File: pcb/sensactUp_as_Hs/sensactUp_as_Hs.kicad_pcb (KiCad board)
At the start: 2 copper layers, 100 x 86.5 mm, 42 parts, among them J1 EXT_ROT, J2 SensactBusConnector, J3 24V+CAN IN, J4 24V+CAN OUT, J5 24V+CAN OUT, J6 24V+CAN OUT, J7 12V LED, Q1 AO3400A, Q2 AO3400A, Q3 AO3400A, SW1 EC11, SW3 TERM OFF, U1 DS18B20, U2 ESP32-S3-DevKitC, U3 DCDC_MP2315, U4 DCDC_MP2315, U5 SN65HVD230, U6 PCA9685PW

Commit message: sensactUp-as_HS updates
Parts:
- added C6: u1, Capacitor_SMD:C_0805_2012Metric_Pad1.18x1.45mm_HandSolder, B.Cu at (120.3, 91.0)
- added C7: 1u, Capacitor_SMD:C_0805_2012Metric_Pad1.18x1.45mm_HandSolder, B.Cu at (118.2, 91.0)
- added J10: OUT0-3, liebler_CONN:PhoenixContact_MCV_1,5_4-G-3.5_1x04_P3.50mm_Vertical_smallerCourtyard, F.Cu at (111.7, 113.1)
- added J11: OUT0-3, liebler_CONN:PhoenixContact_MCV_1,5_4-G-3.5_1x04_P3.50mm_Vertical_smallerCourtyard, F.Cu at (140.9, 113.1)
- added J12: OUT0-3, liebler_CONN:PhoenixContact_MC_1,5_4-G-3.5_1x04_P3.50mm_Horizontal_smallerCourtyard, F.Cu at (141.0, 64.8)
- added J13: OUT0-3, liebler_CONN:PhoenixContact_MCV_1,5_4-G-3.5_1x04_P3.50mm_Vertical_smallerCourtyard, F.Cu at (141.0, 83.3)
- added J14: OUT0-3, liebler_CONN:PhoenixContact_MCV_1,5_4-G-3.5_1x04_P3.50mm_Vertical_smallerCourtyard, F.Cu at (111.7, 83.9)
- added J15: Conn_01x04, Connector_PinHeader_2.54mm:PinHeader_1x04_P2.54mm_Vertical, F.Cu at (137.1, 118.0)
- added J16: Conn_01x04, Connector_PinHeader_2.54mm:PinHeader_1x04_P2.54mm_Vertical, F.Cu at (107.9, 118.0)
- added J17: Conn_01x04, Connector_PinHeader_2.54mm:PinHeader_1x04_P2.54mm_Vertical, F.Cu at (107.9, 103.4)
- added J18: Conn_01x04, Connector_PinHeader_2.54mm:PinHeader_1x04_P2.54mm_Vertical, F.Cu at (115.5, 61.6)
- added J19: Conn_01x04, Connector_PinHeader_2.54mm:PinHeader_1x04_P2.54mm_Vertical, F.Cu at (144.8, 67.8)
- added J20: Conn_01x04, Connector_PinHeader_2.54mm:PinHeader_1x04_P2.54mm_Vertical, F.Cu at (137.2, 88.2)
- added J21: Conn_01x04, Connector_PinHeader_2.54mm:PinHeader_1x04_P2.54mm_Vertical, F.Cu at (107.9, 88.8)
- added J8: OUT0-3, liebler_CONN:PhoenixContact_MCV_1,5_4-G-3.5_1x04_P3.50mm_Vertical_smallerCourtyard, F.Cu at (140.9, 97.9)
- added J9: OUT0-3, liebler_CONN:PhoenixContact_MCV_1,5_4-G-3.5_1x04_P3.50mm_Vertical_smallerCourtyard, F.Cu at (111.7, 98.5)
- added U7: PCA9555PW, liebler_SEMICONDUCTORS:TSSOP-24_4.4x7.8mm_Pitch0.65mm_handsolder, B.Cu at (114.6, 74.0)
- J1: value EXT_ROT -> Conn_01x04; footprint Connector_Phoenix_MC:PhoenixContact_MCV_1,5_4-G-3.5_1x04_P3.50mm_Vertical -> Connector_PinHeader_2.54mm:PinHeader_1x04_P2.54mm_Vertical
- J5: value 24V+CAN OUT -> EXT_ENC
- J6: value 24V+CAN OUT -> OUT0-3
- R8, R9: value 10k -> 4k7
- U6: footprint Package_SO:TSSOP-28_4.4x9.7mm_P0.65mm -> liebler_SEMICONDUCTORS:TSSOP-28_4.4x9.7mm_Pitch0.65mm_handsolder
- moved J7 70.5 mm to (140.9, 135.3), turned to 0 degrees
- moved U4 69.7 mm to (126.0, 119.4)
- moved Q1 63.4 mm to (138.6, 131.0), turned to -90 degrees
- moved Q3 63.2 mm to (146.6, 131.0), turned to -90 degrees
- moved Q2 62.3 mm to (142.6, 131.0), turned to -90 degrees
- moved R12 60.3 mm to (138.6, 127.3), turned to 0 degrees
- moved R16 54.9 mm to (146.6, 127.3), turned to 0 degrees
- moved R14 54.0 mm to (142.6, 127.3), turned to 0 degrees
- moved R15 50.6 mm to (145.6, 124.4), turned to -90 degrees
- moved J1 47.9 mm to (137.1, 102.8), turned to 90 degrees
- moved R13 47.4 mm to (141.7, 124.4), turned to -90 degrees
- moved R11 47.2 mm to (137.6, 124.4), turned to -90 degrees
- moved R7 45.2 mm to (103.1, 78.0), turned to 90 degrees
- moved U1 40.3 mm to (100.2, 79.6), turned to 90 degrees
- moved C5 16.0 mm to (108.2, 76.7), turned to 180 degrees
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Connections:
- J1 pad 1: /A -> /L2
- J1 pad 2: GND -> /L1
- J1 pad 3: /B -> /L0
- J1 pad 4: /S -> GND
- J5 pad 1: unconnected-(J5-Pin_1-Pad1) -> ROT_A
- J5 pad 2: unconnected-(J5-Pin_2-Pad2) -> ROT_B
- J5 pad 3: unconnected-(J5-Pin_3-Pad3) -> PROG_IO0
- J5 pad 4: unconnected-(J5-Pin_4-Pad4) -> GND
- J6 pad 1: unconnected-(J6-Pin_1-Pad1) -> /T2
- J6 pad 2: unconnected-(J6-Pin_2-Pad2) -> /T1
- J6 pad 3: unconnected-(J6-Pin_3-Pad3) -> /T0
- J6 pad 4: unconnected-(J6-Pin_4-Pad4) -> GND
- R11 pad 1: PWM0 -> /L8
- R13 pad 1: PWM1 -> /L7
- R15 pad 1: PWM2 -> /L6
- U2 pad 35: unconnected-(U2-GPIO38-Pad35) -> Onewire
- U2 pad 40: unconnected-(U2-GPIO2/ADC1_CH1-Pad40) -> SDA
- U2 pad 41: unconnected-(U2-GPIO1/ADC1_CH0-Pad41) -> SCL
- U6 pad 10: unconnected-(U6-LED4-Pad10) -> /L4
- U6 pad 11: unconnected-(U6-LED5-Pad11) -> /L5
- U6 pad 12: unconnected-(U6-LED6-Pad12) -> /L6
- U6 pad 13: unconnected-(U6-LED7-Pad13) -> /L7
- U6 pad 15: unconnected-(U6-LED8-Pad15) -> /L8
- U6 pad 16: unconnected-(U6-LED9-Pad16) -> /L9
- U6 pad 17: unconnected-(U6-LED10-Pad17) -> /L10
- U6 pad 18: unconnected-(U6-LED11-Pad18) -> /L11
- U6 pad 19: unconnected-(U6-LED12-Pad19) -> /L12
- U6 pad 20: unconnected-(U6-LED13-Pad20) -> /L13
- U6 pad 21: unconnected-(U6-LED14-Pad21) -> /L14
- U6 pad 22: unconnected-(U6-LED15-Pad22) -> /L15
- U6 pad 6: unconnected-(U6-LED0-Pad6) -> /L0
- U6 pad 7: unconnected-(U6-LED1-Pad7) -> /L1
- U6 pad 8: unconnected-(U6-LED2-Pad8) -> /L2
- U6 pad 9: unconnected-(U6-LED3-Pad9) -> /L3
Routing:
- net +3V3: track 25.7 -> 233.6 mm, vias 0 -> 4
- net SDA: track 0.00 -> 145.2 mm
- net SCL: track 0.00 -> 143.4 mm
- net +24V: track 75.2 -> 174.8 mm
- net PROG_IO0: track 1.90 -> 93.2 mm
- net ROT_B: track 2.43 -> 51.6 mm
- net /T6: track 0.00 -> 42.3 mm
- net /T7: track 0.00 -> 39.3 mm
- net GND: track 2.53 -> 39.6 mm, vias 0 -> 111
- net /T5: track 0.00 -> 36.9 mm
- net /L6: track 0.00 -> 35.3 mm
- net Onewire: track 0.00 -> 35.3 mm
- net /T4: track 0.00 -> 34.4 mm
- net ROT_A: track 2.41 -> 35.9 mm
- net /L8: track 0.00 -> 33.3 mm
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- added copper zone on B.Cu, net GND
- added copper zone on F.Cu, net GND
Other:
- board text added: "12V"
- board text added: "24V"
- board text added: "CANH"
- board text added: "CANL"
- board text added: "GND"
- board text added: "L0"
- board text added: "L1"
- board text added: "L10"
- board text added: "L11"
- board text added: "L12"
- board text added: "L13"
- board text added: "L14"
- board text added: "L2"
- board text added: "L3"
- board text added: "L4"
- board text added: "L5"
- board text added: "L6"
- board text added: "L7"
- board text added: "L8"
- board text added: "L9"
- board text added: "ON TERM OFF"
- board text added: "ROTA"
- board text added: "ROTB"
- board text added: "SW"
- board text added: "T0"
- board text added: "T1"
- board text added: "T10"
- board text added: "T11"
- board text added: "T2"
- board text added: "T3"
- board text added: "T4"
- board text added: "T5"
- board text added: "T6"
- board text added: "T7"
- board text added: "T8"
- board text added: "T9"

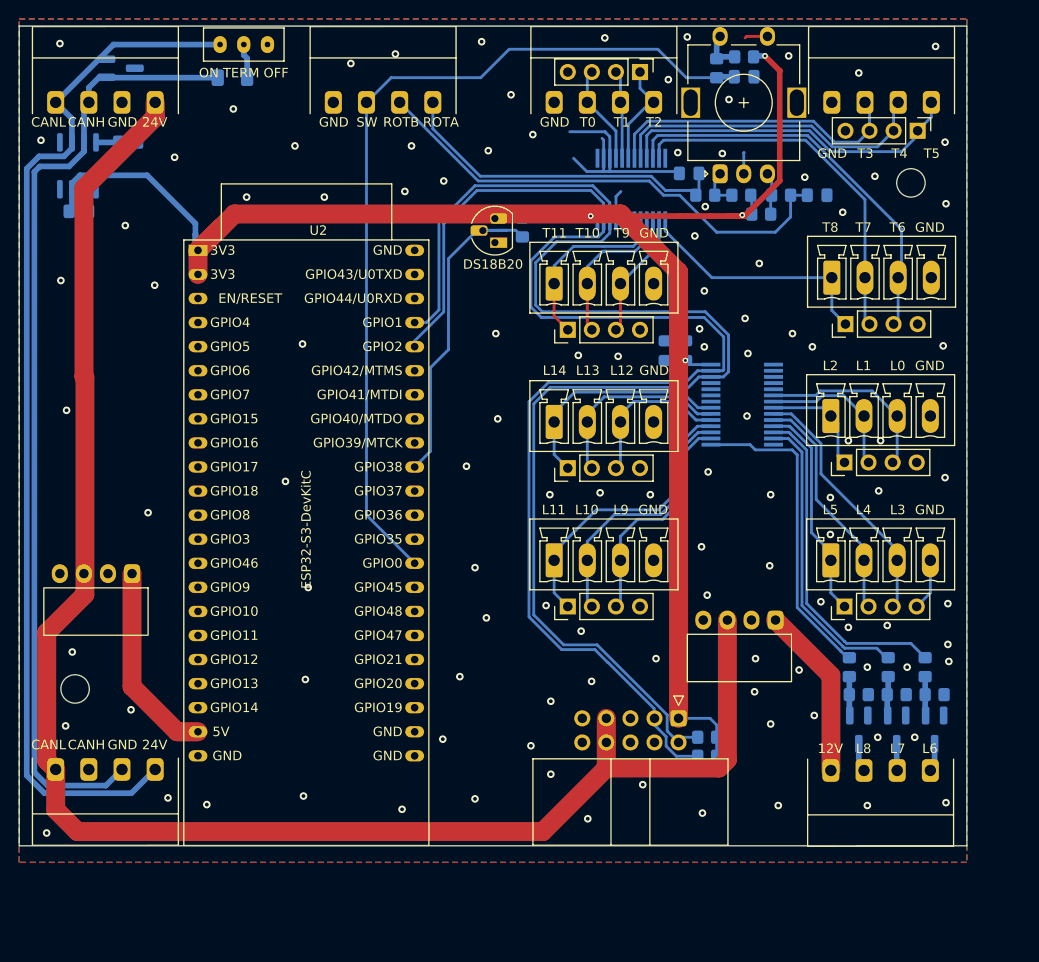
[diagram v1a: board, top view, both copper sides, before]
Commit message: Pin usage according to sensactRingEncoder
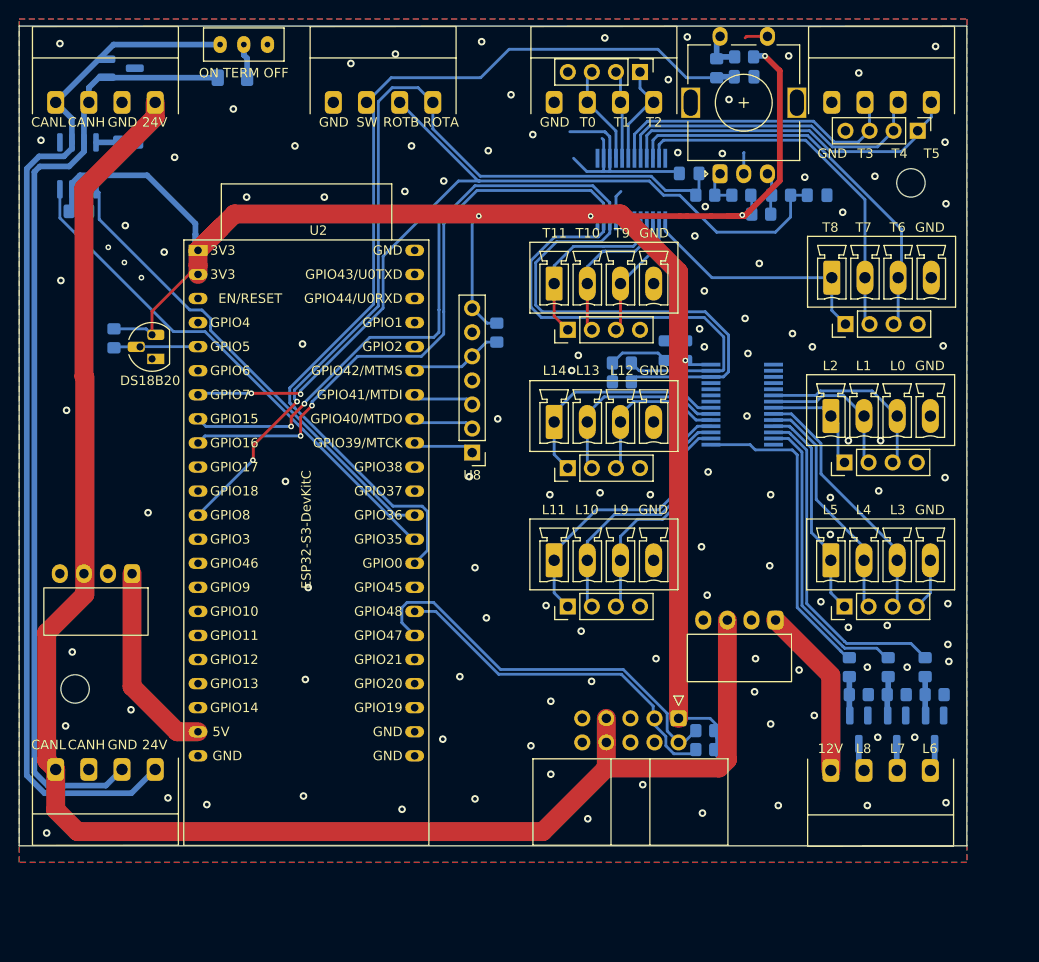
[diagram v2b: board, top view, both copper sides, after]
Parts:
- added R18: 1M, Resistor_SMD:R_0805_2012Metric_Pad1.20x1.40mm_HandSolder, B.Cu at (100.4, 89.1)
- added R19: 4k7, Resistor_SMD:R_0805_2012Metric_Pad1.20x1.40mm_HandSolder, B.Cu at (122.4, 133.1)
- added R20: 4k7, Resistor_SMD:R_0805_2012Metric_Pad1.20x1.40mm_HandSolder, B.Cu at (122.4, 131.1)
- added U8: MAX98357_MODULE, Connector_PinHeader_2.54mm:PinHeader_1x07_P2.54mm_Vertical, F.Cu at (97.8, 101.8)
- moved R7 44.7 mm to (60.0, 89.7)
- moved R9 42.5 mm to (113.6, 92.3), turned to 0 degrees
- moved R8 38.6 mm to (113.6, 94.3), turned to 0 degrees
- moved U1 38.2 mm to (64.0, 91.9)
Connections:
- J2 pad 2: SCL -> SCL_EXT
- J2 pad 3: SDA -> SDA_EXT
- U2 pad 10: unconnected-(U2-GPIO17/ADC2_CH6-Pad10) -> LCD_TRST
- U2 pad 11: unconnected-(U2-GPIO18/ADC2_CH7-Pad11) -> LCD_TINT
- U2 pad 12: unconnected-(U2-GPIO8/ADC1_CH7-Pad12) -> ROT_A
- U2 pad 15: unconnected-(U2-GPIO9/ADC1_CH8-Pad15) -> LCD_BL
- U2 pad 16: unconnected-(U2-GPIO10/ADC1_CH9-Pad16) -> LCD_RS
- U2 pad 17: unconnected-(U2-GPIO11/ADC2_CH0-Pad17) -> LCD_CS
- U2 pad 18: unconnected-(U2-GPIO12/ADC2_CH1-Pad18) -> LCD_SCK
- U2 pad 19: unconnected-(U2-GPIO13/ADC2_CH2-Pad19) -> LCD_DAT
- U2 pad 20: unconnected-(U2-GPIO14/ADC2_CH3-Pad20) -> LCD_RESET
- U2 pad 27: unconnected-(U2-GPIO21-Pad27) -> BaseIO1
- U2 pad 28: unconnected-(U2-GPIO47-Pad28) -> SCL_EXT
- U2 pad 29: unconnected-(U2-GPIO48-Pad29) -> SDA_EXT
- U2 pad 32: unconnected-(U2-GPIO35-Pad32) -> CAN_RX
- U2 pad 33: unconnected-(U2-GPIO36-Pad33) -> CAN_TX
- U2 pad 35: Onewire -> unconnected-(U2-GPIO38-Pad35)
- U2 pad 36: unconnected-(U2-GPIO39/MTCK-Pad36) -> I2S_FS
- U2 pad 37: unconnected-(U2-GPIO40/MTDO-Pad37) -> I2S_BCLK
- U2 pad 38: unconnected-(U2-GPIO41/MTDI-Pad38) -> I2S_DAC
- U2 pad 39: unconnected-(U2-GPIO42/MTMS-Pad39) -> AMP_SD
- U2 pad 40: SDA -> MIC_CLK
- U2 pad 41: SCL -> MIC_DAT
- U2 pad 5: unconnected-(U2-GPIO5/ADC1_CH4-Pad5) -> Onewire
- U2 pad 7: unconnected-(U2-GPIO7/ADC1_CH6-Pad7) -> ROT_B
- U2 pad 8: unconnected-(U2-GPIO15/ADC2_CH4/32K_P-Pad8) -> SCL
- U2 pad 9: unconnected-(U2-GPIO16/ADC2_CH5/32K_N-Pad9) -> SDA
- U5 pad 1: CANT -> CAN_TX
- U5 pad 4: CANR -> CAN_RX
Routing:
- net ROT_A: track 35.9 -> 94.6 mm, vias 0 -> 2
- net CAN_RX: track 0.00 -> 54.5 mm
- net CAN_TX: track 0.00 -> 52.2 mm
- net ROT_B: track 51.6 -> 94.2 mm, vias 0 -> 2
- net SCL_EXT: track 0.00 -> 42.0 mm
- net SDA_EXT: track 0.00 -> 37.4 mm
- net +3V3: track 233.6 -> 266.0 mm, vias 4 -> 5
- net SDA: track 145.2 -> 114.7 mm, vias 0 -> 2
- net SCL: track 143.4 -> 115.6 mm, vias 0 -> 2
- net Onewire: track 35.3 -> 8.92 mm
- net PROG_IO0: track 93.2 -> 103.4 mm
- net AMP_SD: track 0.00 -> 9.92 mm
- net I2S_FS: track 0.00 -> 6.49 mm
- net I2S_DAC: track 0.00 -> 6.49 mm
- net I2S_BCLK: track 0.00 -> 6.49 mm
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
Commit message: sensactUp_as_Hs
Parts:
- removed C7: 1u, Capacitor_SMD:C_0805_2012Metric_Pad1.18x1.45mm_HandSolder
- removed J1, J15, J16, J17, J18, J19, J20, J21: Conn_01x04, Connector_PinHeader_2.54mm:PinHeader_1x04_P2.54mm_Vertical
- removed J13, J14: OUT0-3, liebler_CONN:PhoenixContact_MCV_1,5_4-G-3.5_1x04_P3.50mm_Vertical_smallerCourtyard
- removed Q1, Q2, Q3: AO3400A, Package_TO_SOT_SMD:SOT-23_Handsoldering
- removed SW1: EC11, liebler_MECH:RotaryEncoder_Alps_EC11E-Switch_Vertical_H20mm
- removed U6: PCA9685PW, liebler_SEMICONDUCTORS:TSSOP-28_4.4x9.7mm_Pitch0.65mm_handsolder
- added C10: 10n, Capacitor_SMD:C_0805_2012Metric_Pad1.18x1.45mm_HandSolder, B.Cu at (72.0, 103.8)
- added C11: 10n, Capacitor_SMD:C_0805_2012Metric_Pad1.18x1.45mm_HandSolder, B.Cu at (72.0, 93.7)
- added C12: 10n, Capacitor_SMD:C_0805_2012Metric_Pad1.18x1.45mm_HandSolder, B.Cu at (72.0, 101.3)
- added C8: u1, Capacitor_SMD:C_0805_2012Metric_Pad1.18x1.45mm_HandSolder, B.Cu at (102.4, 67.3)
- added C9: u1, Capacitor_SMD:C_0805_2012Metric_Pad1.18x1.45mm_HandSolder, B.Cu at (119.5, 66.2)
- added U10: TPL7407LAPW, Package_SO:TSSOP-16_4.4x5mm_P0.65mm, B.Cu at (123.2, 72.3)
- added U11: DS2482, liebler_SEMICONDUCTORS:SOIC-8_3.9x4.9mm_P1.27mm_handsolder, B.Cu at (98.8, 111.5)
- added U9: TPL7407LAPW, Package_SO:TSSOP-16_4.4x5mm_P0.65mm, B.Cu at (106.8, 72.3)
- J10: value OUT0-3 -> ROT1; footprint liebler_CONN:PhoenixContact_MCV_1,5_4-G-3.5_1x04_P3.50mm_Vertical_smallerCourtyard -> liebler_CONN:PhoenixContact_MCV_1,5_5-G-3.81_1x05_P3.81mm_Vertical_smallerCourtyard
- J11: value OUT0-3 -> OneWire; footprint liebler_CONN:PhoenixContact_MCV_1,5_4-G-3.5_1x04_P3.50mm_Vertical_smallerCourtyard -> liebler_CONN:PhoenixContact_MCV_1,5_5-G-3.81_1x05_P3.81mm_Vertical_smallerCourtyard
- J12: value OUT0-3 -> LED Driver; footprint liebler_CONN:PhoenixContact_MC_1,5_4-G-3.5_1x04_P3.50mm_Horizontal_smallerCourtyard -> Connector_PinHeader_2.54mm:PinHeader_1x08_P2.54mm_Vertical
- J3: footprint liebler_CONN:PhoenixContact_MC_1,5_4-G-3.5_1x04_P3.50mm_Horizontal_smallerCourtyard -> liebler_CONN:PhoenixContact_MCV_1,5_4-G-3.5_1x04_P3.50mm_Vertical_smallerCourtyard
- J4: value 24V+CAN OUT -> LED; footprint liebler_CONN:PhoenixContact_MC_1,5_4-G-3.5_1x04_P3.50mm_Horizontal_smallerCourtyard -> liebler_CONN:PhoenixContact_MCV_1,5_5-G-3.81_1x05_P3.81mm_Vertical_smallerCourtyard
- J5: value EXT_ENC -> ROT2; footprint liebler_CONN:PhoenixContact_MC_1,5_4-G-3.5_1x04_P3.50mm_Horizontal_smallerCourtyard -> liebler_CONN:PhoenixContact_MCV_1,5_5-G-3.81_1x05_P3.81mm_Vertical_smallerCourtyard
- J6: value OUT0-3 -> LED Driver; footprint liebler_CONN:PhoenixContact_MC_1,5_4-G-3.5_1x04_P3.50mm_Horizontal_smallerCourtyard -> liebler_CONN:PhoenixContact_MC_0,5_8-G-2.5_1x08_P2.50mm_Horizontal
- J7: value 12V LED -> LED; footprint liebler_CONN:PhoenixContact_MC_1,5_4-G-3.5_1x04_P3.50mm_Horizontal_smallerCourtyard -> liebler_CONN:PhoenixContact_MCV_1,5_5-G-3.81_1x05_P3.81mm_Vertical_smallerCourtyard
- J8, J9: value OUT0-3 -> LED; footprint liebler_CONN:PhoenixContact_MCV_1,5_4-G-3.5_1x04_P3.50mm_Vertical_smallerCourtyard -> liebler_CONN:PhoenixContact_MCV_1,5_5-G-3.81_1x05_P3.81mm_Vertical_smallerCourtyard
- R11, R13, R15: value k1 -> 10k
- U2: footprint Espressif:ESP32-S3-DevKitC -> liebler_MODULES:ESP32-S3 chinese dev board
- U3, U4: footprint liebler_MODULES:DCDC_MP2315 -> liebler_MODULES:DCDC_MP2315_horizontal
- U7: value PCA9555PW -> PCA9685PW; footprint liebler_SEMICONDUCTORS:TSSOP-24_4.4x7.8mm_Pitch0.65mm_handsolder -> liebler_SEMICONDUCTORS:TSSOP-28_4.4x9.7mm_Pitch0.65mm_handsolder
- moved J4 114.6 mm to (145.6, 60.1), turned to 180 degrees
- moved R14 92.7 mm to (63.1, 79.6), turned to 180 degrees
- moved R16 92.1 mm to (62.8, 89.2), turned to 180 degrees
- moved R13 91.4 mm to (63.1, 77.7), turned to 180 degrees
- moved R15 89.2 mm to (62.8, 91.1), turned to 180 degrees
- moved R12 83.2 mm to (62.8, 93.0), turned to 180 degrees
- moved R11 80.4 mm to (62.8, 94.9), turned to 180 degrees
- moved J7 77.4 mm to (122.6, 60.1), turned to 180 degrees
- moved SW3 75.7 mm to (62.3, 133.6), turned to 0 degrees
- moved D1 75.7 mm to (55.9, 136.7), turned to 180 degrees
- moved R17 75.4 mm to (61.1, 136.7)
- moved J3 75.0 mm to (59.4, 139.8), turned to 0 degrees
- moved J6 71.5 mm to (127.7, 134.5), turned to 0 degrees
- moved R4 68.5 mm to (62.8, 96.8), turned to 180 degrees
- moved R2 68.1 mm to (63.1, 85.3)
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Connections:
- C1 pad 2: ROT_A -> ROT2_A
- C2 pad 2: ROT_B -> ROT1_A
- C3 pad 1: PROG_IO0 -> GND
- C3 pad 2: GND -> ROT1_B
- J10 pad 1: /L11 -> GND
- J10 pad 2: /L10 -> GND
- J10 pad 3: /L9 -> ROT1_SS
- J10 pad 4: GND -> ROT1_BB
- J11 pad 1: /L5 -> +24V
- J11 pad 2: /L4 -> +12V
- J11 pad 3: /L3 -> +3V3
- J11 pad 4: GND -> Net-(J11-Pin_4)
- J12 pad 1: /T5 -> /L5
- J12 pad 2: /T4 -> /L4
- J12 pad 3: /T3 -> /L3
- J12 pad 4: GND -> /L2
- J3 pad 1: +24V -> GND
- J3 pad 2: GND -> CANL
- J3 pad 4: CANL -> +24V
- J4 pad 1: +24V -> LED11
- J4 pad 2: GND -> LED10
- J4 pad 3: CANH -> LED9
- J4 pad 4: CANL -> LED8
- J5 pad 1: ROT_A -> GND
- J5 pad 2: ROT_B -> GND
- J5 pad 3: PROG_IO0 -> ROT2_SS
- J5 pad 4: GND -> ROT2_BB
- J6 pad 1: /T2 -> /L5
- J6 pad 2: /T1 -> /L4
- J6 pad 3: /T0 -> /L3
- J6 pad 4: GND -> /L2
- J7 pad 1: +12V -> LED7
- J7 pad 2: Net-(J7-Pin_2) -> LED6
- J7 pad 3: Net-(J7-Pin_3) -> LED5
- J7 pad 4: Net-(J7-Pin_4) -> LED4
- J8 pad 1: /L2 -> LED12
- J8 pad 2: /L1 -> LED13
- J8 pad 3: /L0 -> LED_G_14
- J8 pad 4: GND -> LED_G_15
- J9 pad 1: /L14 -> LED3
- J9 pad 2: /L13 -> LED2
- J9 pad 3: /L12 -> LED1
- J9 pad 4: GND -> LED0
- R1 pad 1: ROT_A -> ROT2_A
- R1 pad 2: /A -> ROT2_AA
- R11 pad 1: /L8 -> ROT2_B
- R11 pad 2: Net-(Q1-G) -> ROT2_BB
- R12 pad 1: Net-(Q1-G) -> +3V3
- R12 pad 2: GND -> ROT2_BB
- R13 pad 1: /L7 -> ROT1_S
- R13 pad 2: Net-(Q2-G) -> ROT1_SS
- R14 pad 1: Net-(Q2-G) -> +3V3
- R14 pad 2: GND -> ROT1_SS
- R15 pad 1: /L6 -> ROT2_S
- R15 pad 2: Net-(Q3-G) -> ROT2_SS
- R16 pad 1: Net-(Q3-G) -> +3V3
- R16 pad 2: GND -> ROT2_SS
- R2 pad 1: ROT_B -> ROT1_A
- R2 pad 2: /B -> ROT1_AA
- R3 pad 2: /A -> ROT1_AA
- R4 pad 2: /B -> ROT2_AA
- R5 pad 1: +3V3 -> ROT1_B
- R5 pad 2: /S -> ROT1_BB
- R6 pad 1: PROG_IO0 -> +3V3
- R6 pad 2: /S -> ROT1_BB
- SW3 pad 1: unconnected-(SW3-A-Pad1) -> CANH
- U2 pad 10: LCD_TRST -> /L1
- U2 pad 11: LCD_TINT -> /L2
- U2 pad 12: ROT_A -> /L4
- U2 pad 13: unconnected-(U2-GPIO3/ADC1_CH2-Pad13) -> Onewire
- U2 pad 15: LCD_BL -> INT0
- U2 pad 16: LCD_RS -> INT2
- U2 pad 17: LCD_CS -> CAN_RX
- U2 pad 18: LCD_SCK -> CAN_TX
- U2 pad 19: LCD_DAT -> SDA_EXT
- U2 pad 20: LCD_RESET -> SCL_EXT
- U2 pad 27: BaseIO1 -> INT1
- U2 pad 28: SCL_EXT -> /L5
- U2 pad 29: SDA_EXT -> /L3
- U2 pad 31: PROG_IO0 -> unconnected-(U2-GPIO0-Pad31)
- U2 pad 32: CAN_RX -> /L0
- U2 pad 33: CAN_TX -> unconnected-(U2-GPIO36-Pad33)
- U2 pad 34: unconnected-(U2-GPIO37-Pad34) -> SCL
- U2 pad 35: unconnected-(U2-GPIO38-Pad35) -> SDA
- U2 pad 4: unconnected-(U2-GPIO4/ADC1_CH3-Pad4) -> ROT1_S
- U2 pad 40: MIC_CLK -> unconnected-(U2-GPIO2/ADC1_CH1-Pad40)
- U2 pad 41: MIC_DAT -> +3V3
- U2 pad 5: Onewire -> ROT1_B
- U2 pad 6: unconnected-(U2-GPIO6/ADC1_CH5-Pad6) -> ROT1_A
- U2 pad 7: ROT_B -> ROT2_S
- U2 pad 8: SCL -> ROT2_B
- U2 pad 9: SDA -> ROT2_A
- U7 pad 1: unconnected-(U7-~{INT}-Pad1) -> +3V3
- U7 pad 10: /T6 -> LED_G_4
- U7 pad 11: /T7 -> LED_G_5
- U7 pad 12: GND -> LED_G_6
- U7 pad 13: /T8 -> LED_G_7
- U7 pad 14: /T9 -> GND
- U7 pad 15: /T10 -> LED_G_8
- U7 pad 16: /T11 -> LED_G_9
- U7 pad 17: /T12 -> LED_G_10
- U7 pad 18: /T13 -> LED_G_11
- U7 pad 19: /T14 -> LED_G_12
- U7 pad 20: unconnected-(U7-IO1_7-Pad20) -> LED_G_13
- U7 pad 21: GND -> LED_G_14
- U7 pad 22: SCL -> LED_G_15
- U7 pad 23: SDA -> GND
- U7 pad 24: +3V3 -> GND
- U7 pad 4: /T0 -> GND
- U7 pad 5: /T1 -> GND
- U7 pad 6: /T2 -> LED_G_0
- U7 pad 7: /T3 -> LED_G_1
- U7 pad 8: /T4 -> LED_G_2
- U7 pad 9: /T5 -> LED_G_3
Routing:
- net +12V: track 18.3 -> 160.0 mm, vias 0 -> 1
- net PROG_IO0: track 103.4 -> 0.00 mm
- net ROT_A: track 94.6 -> 0.00 mm, vias 2 -> 0
- net ROT_B: track 94.2 -> 0.00 mm, vias 2 -> 0
- net CANL: track 110.5 -> 21.1 mm
- net CANH: track 101.0 -> 14.2 mm
- net /L1: track 15.8 -> 86.6 mm
- net /L2: track 11.9 -> 82.3 mm
- net SDA: track 114.7 -> 49.2 mm, vias 2 -> 0
- net SCL: track 115.6 -> 50.3 mm, vias 2 -> 0
- net INT0: track 0.00 -> 53.6 mm
- net /L4: track 24.9 -> 76.6 mm
- net +24V: track 174.8 -> 123.2 mm
- net +3V3: track 266.0 -> 214.4 mm, vias 5 -> 4
- net INT2: track 0.00 -> 50.9 mm
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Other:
- board text added: "1Wire"
- board text added: "3V"
- board text added: "A"
- board text added: "B"
- board text added: "LED0"
- board text added: "LED1"
- board text added: "LED2"
- board text added: "LED3"
- board text added: "LED4"
- board text added: "LED5"
- board text added: "LED6"
- board text added: "LED7"
- board text added: "LED8"
- board text added: "LED9"
- board text added: "LEDA"
- board text added: "LEDB"
- board text added: "LEDC"
- board text added: "LEDD"
- board text added: "LEDE"
- board text added: "LEDF"
- board text added: "S"
- board text added: "TERM ON"
- board text removed: "L10"
- board text removed: "L11"
- board text removed: "L12"
- board text removed: "L13"
- board text removed: "L14"
- board text removed: "L6"
- board text removed: "L7"
- board text removed: "L8"
- board text removed: "L9"
- board text removed: "ON TERM OFF"
- board text removed: "ROTA"
- board text removed: "ROTB"
- board text removed: "SW"
- board text removed: "T0"
- board text removed: "T1"
- board text removed: "T10"
- board text removed: "T11"
- board text removed: "T2"
- board text removed: "T3"
- board text removed: "T4"
- board text removed: "T5"
- board text removed: "T6"
- board text removed: "T7"
- board text removed: "T8"
- board text removed: "T9"

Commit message: PCB for sensactUp_as_Hs as odered @ JLCPCB
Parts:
- removed R7: 1k, Resistor_SMD:R_0805_2012Metric_Pad1.20x1.40mm_HandSolder
- added C7: u1, Capacitor_SMD:C_0805_2012Metric_Pad1.18x1.45mm_HandSolder, B.Cu at (77.2, 114.7)
- added J1: 5V OUT, liebler_CONN:PhoenixContact_MCV_1,5_5-G-3.81_1x05_P3.81mm_Vertical_smallerCourtyard, F.Cu at (145.6, 113.7)
- added U6: 74AHCT125, liebler_SEMICONDUCTORS:SOIC-14_3.9x8.7mm_P1.27mm_handsolder, B.Cu at (82.8, 114.8)
- moved U1 48.5 mm to (111.0, 101.3), turned to 0 degrees
- moved C4 14.0 mm to (113.7, 104.6)
- moved U11 10.3 mm to (107.8, 106.5), turned to 180 degrees
- moved R17 0.30 mm to (61.1, 136.4)
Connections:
- J11 pad 4: Net-(J11-Pin_4) -> OneWireExt
- U1 pad 2: Onewire -> OneWireExt
- U11 pad 2: Net-(J11-Pin_4) -> OneWireExt
- U2 pad 10: /L1 -> RGB_22
- U2 pad 11: /L2 -> /L1
- U2 pad 12: /L4 -> /L2
- U2 pad 13: Onewire -> /L4
- U2 pad 33: unconnected-(U2-GPIO36-Pad33) -> RGB_11
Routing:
- net RGB_2: track 0.00 -> 64.6 mm
- net RGB_1: track 0.00 -> 64.5 mm
- net +12V: track 160.0 -> 189.3 mm
- net OneWireExt: track 0.00 -> 19.6 mm
- net +5V: track 32.1 -> 50.9 mm, vias 0 -> 1
- net Net-(J11-Pin_4): track 14.8 -> 0.00 mm
- net RGB_11: track 0.00 -> 13.2 mm
- net RGB_22: track 0.00 -> 12.5 mm
- net Onewire: track 7.89 -> 0.00 mm
- net +24V: track 123.2 -> 130.8 mm
- net +3V3: track 214.4 -> 212.1 mm, vias 4 -> 6
- net SDA: track 49.2 -> 47.3 mm
- net /L1: track 86.6 -> 85.0 mm
- net SCL: track 50.3 -> 51.8 mm
- net CANH: track 14.2 -> 12.9 mm
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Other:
- board text added: "RGB1"
- board text added: "RGB2"
- board text added: "sensactUp_as_Hs 2025-10-07 Klaus Liebler"
